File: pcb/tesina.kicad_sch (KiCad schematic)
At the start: 12 parts, among them J1 Conn_01x02_Male, J5 AMP2_IN, J6 AMP3_IN, J7 AMP2_OUT, J8 AMP3_OUT

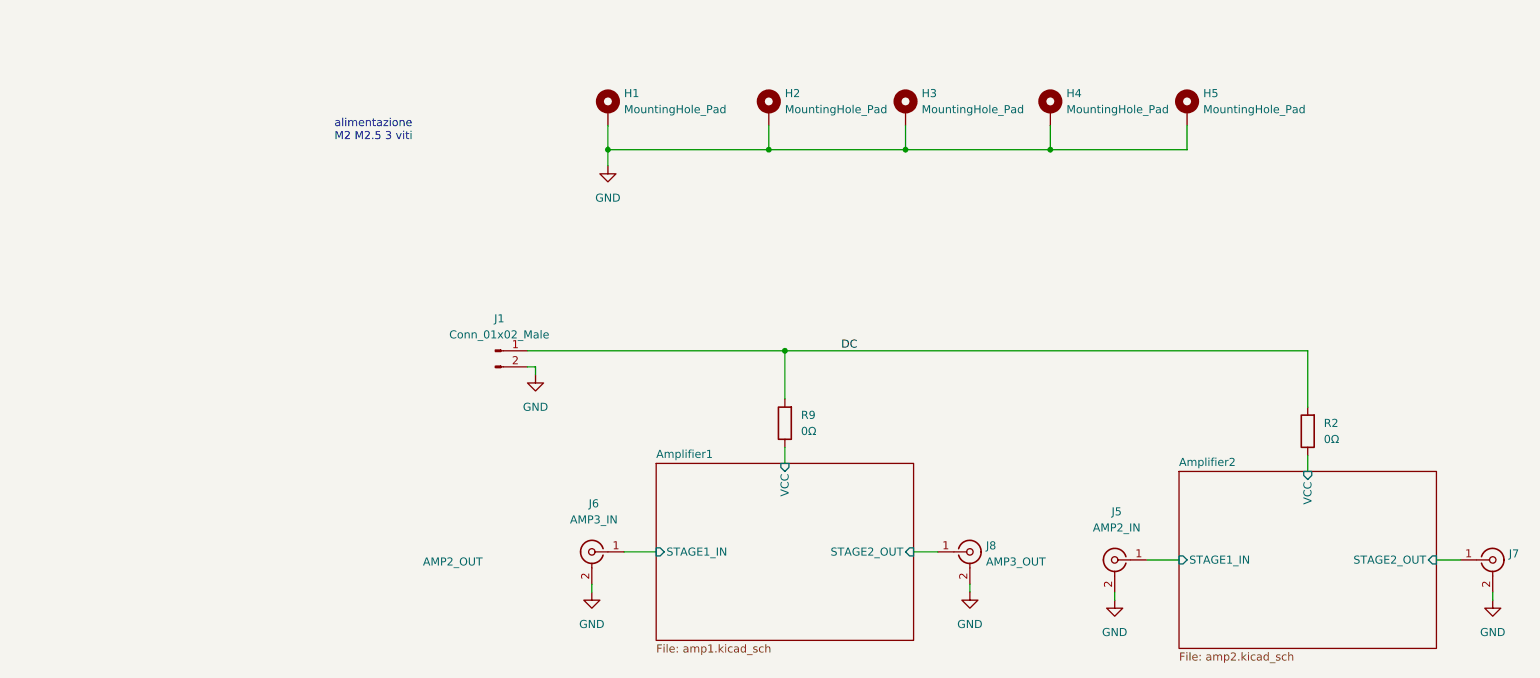
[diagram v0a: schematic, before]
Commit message: PCB modified according to suggestions
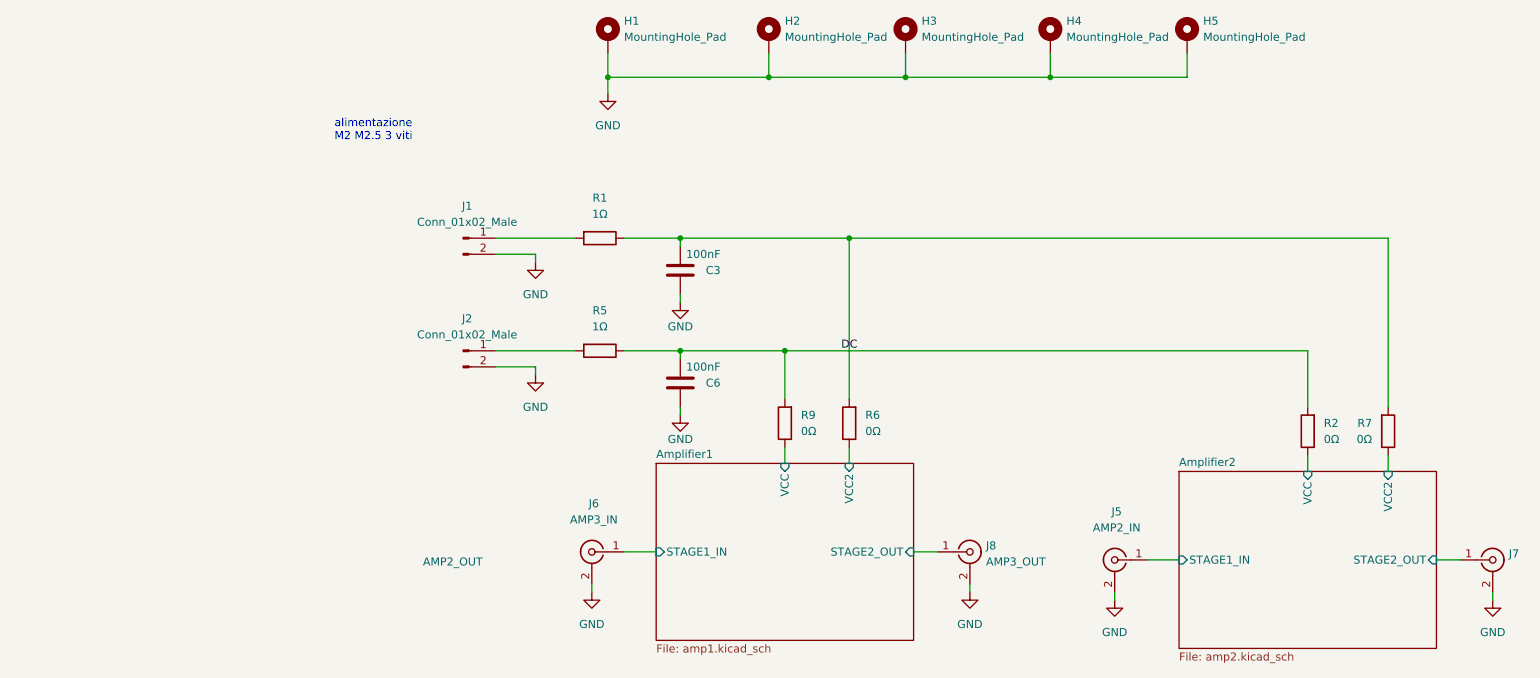
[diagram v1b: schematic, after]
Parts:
- added C3, C6: 100nF, Capacitor_SMD:C_1206_3216Metric, symbol Device:C
- added J2: Conn_01x02_Male, Nicobigio01:Connector_Pad, symbol Connector:Conn_01x02_Male
- added R1, R5: 1Ω, Resistor_SMD:R_0603_1608Metric, symbol Device:R
- added R6, R7: 0Ω, Resistor_SMD:R_0603_1608Metric, symbol Device:R
- J1: footprint Connector_PinHeader_2.54mm:PinHeader_1x02_P2.54mm_Vertical -> Nicobigio01:Connector_Pad
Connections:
- net DC: now also C6.2, R5.1; no longer J1.1 (Pin_1)
- net GND: now also C3.1, C6.1, J2.2 (Pin_2)
- new net: J1.1 (Pin_1), R1.2
- new net: J2.1 (Pin_1), R5.2
- new net: C3.2, R1.1, R6.2, R7.2
- new net Amplifier1/VCC2: R6.1
- new net Amplifier2/VCC2: R7.1
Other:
- sheet Amplifier1 ports: added VCC2; removed none
- sheet Amplifier2 ports: added VCC2; removed none
- moved on the sheet: H1, H2, H3, H4, H5

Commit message: design finished
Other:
- note added: "Togliere condensatore grosso allargare pad net tie stub"
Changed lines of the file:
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@@
+    (effects (font (size 1.27 1.27)) (justify left bottom))
+  )
+  (text "Togliere condensatore grosso\nallargare pad\nnet tie stub\n "
+    (at 30.48 88.9 0)
     (effects (font (size 1.27 1.27)) (justify left bottom))
   )
@@
       (reference "#PWR0111") (unit 1) (value "GND") (footprint "")
     )
-    (path "/87ee7424-77dd-42bb-9d0a-6365445b897a/9b2acd55-d247-4b05-8940-cded0e63ec3f"
-      (reference "#PWR0112") (unit 1) (value "GND") (footprint "")
-    )
-    (path "/87ee7424-77dd-42bb-9d0a-6365445b897a/f10d4adb-f024-4c05-ad2a-4fe8bc51b34a"
-      (reference "#PWR0113") (unit 1) (value "GND") (footprint "")
-    )
     (path "/4e3d076a-abc7-4ccc-a891-541b92d429fd/7953584d-b841-4595-a6d3-d80b17a03b27"
       (reference "#PWR0114") (unit 1) (value "GND") (footprint "")
@@
       (reference "C7") (unit 1) (value "100pF") (footprint "Capacitor_SMD:C_0603_1608Metric")
     )
-    (path "/87ee7424-77dd-42bb-9d0a-6365445b897a/0493fad5-de27-4ec6-ac8b-c4dfccc03df1"
-      (reference "C8") (unit 1) (value "100nF") (footprint "Capacitor_SMD:C_1206_3216Metric")
-    )
     (path "/4e3d076a-abc7-4ccc-a891-541b92d429fd/a8340b88-8d21-4253-a26d-099cf6225b90"
       (reference "C9") (unit 1) (value "1.45pF") (footprint "Capacitor_SMD:C_0603_1608Metric")
     )
-    (path "/87ee7424-77dd-42bb-9d0a-6365445b897a/b3e5b340-bf3e-4659-a25d-0ab99c9efbc9"
-      (reference "C10") (unit 1) (value "100nF") (footprint "Capacitor_SMD:C_1206_3216Metric")
-    )
     (path "/4e3d076a-abc7-4ccc-a891-541b92d429fd/9a1c3504-0cda-4a2b-90da-1f74054da7d2"

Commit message: cleanup
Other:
- note removed: "Togliere condensatore grosso allargare pad net tie stub"
- note removed: "alimentazione M2 M2.5 3 viti"
